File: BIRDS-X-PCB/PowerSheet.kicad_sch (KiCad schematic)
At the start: 31 parts, among them J201 Conn_01x02, J202 Conn_01x02, J203 Conn_01x02, Q201 AO3420, Q202 AO3420, Q502 2N7002, U201 LTC4361-2, U202 LTC4361-2, U203 0.1S7B_0512S3UP

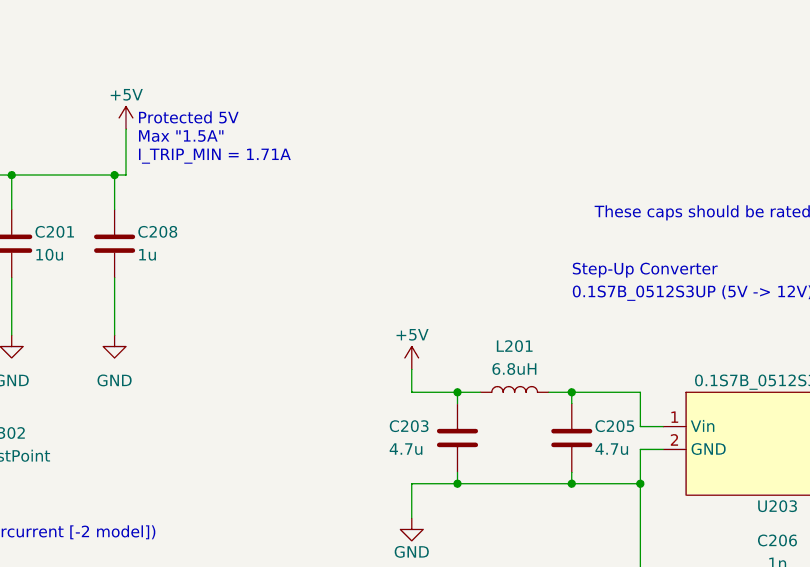
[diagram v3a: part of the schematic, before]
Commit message: Add 12V disable
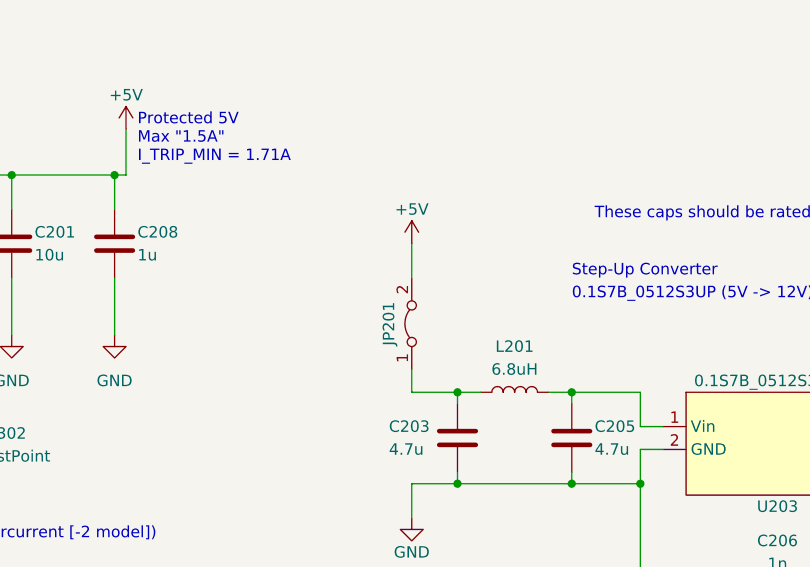
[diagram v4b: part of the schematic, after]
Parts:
- added JP201: Jumper_2_Open, Jumper:SolderJumper-2_P1.3mm_Open_RoundedPad1.0x1.5mm, symbol Jumper:Jumper_2_Bridged
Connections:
- net +5V: now also JP201.2 (B); no longer C203.1, L201.1
- new net: C203.1, JP201.1 (A), L201.1
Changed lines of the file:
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@@
+    (stroke (width 0) (type default))
+  )
+  (wire (pts (xy 161.29 63.5) (xy 161.29 66.04))
     (stroke (width 0) (type default))
   )
@@
     (stroke (width 0) (type default))
   )
-  (wire (pts (xy 161.29 63.5) (xy 161.29 66.04))
+  (wire (pts (xy 161.29 49.53) (xy 161.29 53.34))
     (stroke (width 0) (type default))
   )
@@
         (path "/c2796b15-795a-4d6e-ad4b-0ba87ded4bc9/f0b1214b-f453-423f-b2cf-f5d10e08eafe"
           (reference "#PWR015") (unit 1)
+        )
+      )
+    )
+  )
+  (symbol (lib_id "Jumper:Jumper_2_Bridged") (at 161.29 58.42 90) (unit 1)
+    (in_bom yes) (on_board yes) (dnp no)
+    (property "Reference" "JP201" (at 158.75 58.42 0)
+      (effects (font (size 1.27 1.27)))
+    )
+    (property "Value" "Jumper_2_Open" (at 162.56 60.325 90)
+      (effects (font (size 1.27 1.27)) (justify right) hide)
+    )
+    (property "Footprint" "Jumper:SolderJumper-2_P1.3mm_Open_RoundedPad1.0x1.5mm" (at 161.29 58.42 0)
+      (effects (font (size 1.27 1.27)) hide)
+    )
+    (property "Datasheet" "~" (at 161.29 58.42 0)
+      (effects (font (size 1.27 1.27)) hide)
+    )
+    (pin "1")
+    (pin "2")
+    (instances
+      (project "BIRDS-X-PCB"
+        (path "/c2796b15-795a-4d6e-ad4b-0ba87ded4bc9/f0b1214b-f453-423f-b2cf-f5d10e08eafe"
+          (reference "JP201") (unit 1)
+        )
+        (path "/c2796b15-795a-4d6e-ad4b-0ba87ded4bc9/245c031a-1c72-4f7a-bf07-271990525459"
+          (reference "JP501") (unit 1)
         )
       )
@@
     )
   )
-  (symbol (lib_id "power:+5V") (at 161.29 63.5 0) (unit 1)
-    (in_bom yes) (on_board yes) (dnp no) (fields_autoplaced)
-    (property "Reference" "#PWR07" (at 161.29 67.31 0)
-      (effects (font (size 1.27 1.27)) hide)
-    )
-    (property "Value" "+5V" (at 161.29 59.69 0)
-      (effects (font (size 1.27 1.27)))
-    )
-    (property "Footprint" "" (at 161.29 63.5 0)
-      (effects (font (size 1.27 1.27)) hide)
-    )
-    (property "Datasheet" "" (at 161.29 63.5 0)
-      (effects (font (size 1.27 1.27)) hide)
-    )
+  (symbol (lib_id "power:+5V") (at 161.29 49.53 0) (unit 1)
+    (in_bom yes) (on_board yes) (dnp no) (fields_autoplaced)
+    (property "Reference" "#PWR07" (at 161.29 53.34 0)
+      (effects (font (size 1.27 1.27)) hide)
+    )
+    (property "Value" "+5V" (at 161.29 45.72 0)
+      (effects (font (size 1.27 1.27)))
+    )
+    (property "Footprint" "" (at 161.29 49.53 0)
+      (effects (font (size 1.27 1.27)) hide)
+    )
+    (property "Datasheet" "" (at 161.29 49.53 0)
+      (effects (font (size 1.27 1.27)) hide)
+    )

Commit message: Prep docs for Rev5.1 release
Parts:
- C206, R203, R204, R205: now not fitted
- J201, J202, J203: now not fitted; now left out of the parts list
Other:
- note removed: "TODO switch to one of these if we can order one"
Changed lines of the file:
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@@
   (paper "USLetter")
   (title_block
-    (rev "Rev5.0")
+    (date "2023-09-07")
+    (rev "Rev5.1")
   )
   (junction (at 68.58 50.8) (diameter 0) (color 0 0 0 0)
@@
   (text "For the LTC4361 (per datasheet page 5):\n    R_SENSE = (0.05V) / I_SENSE"
     (at 15.24 20.32 0)
-    (effects (font (size 1.27 1.27)) (justify left bottom))
-  )
-  (text "TODO switch to one of these if we can order one" (at 193.04 104.14 0)
     (effects (font (size 1.27 1.27)) (justify left bottom))
   )
@@
   )
   (symbol (lib_id "Device:R") (at 213.36 130.81 0) (unit 1)
-    (in_bom yes) (on_board yes) (dnp no) (fields_autoplaced)
+    (in_bom yes) (on_board yes) (dnp yes) (fields_autoplaced)
     (property "Reference" "R204" (at 215.9 129.54 0)
       (effects (font (size 1.27 1.27)) (justify left))
@@
   )
   (symbol (lib_id "Device:R") (at 198.12 130.81 0) (unit 1)
-    (in_bom yes) (on_board yes) (dnp no) (fields_autoplaced)
+    (in_bom yes) (on_board yes) (dnp yes) (fields_autoplaced)
     (property "Reference" "R203" (at 200.66 129.54 0)
       (effects (font (size 1.27 1.27)) (justify left))
@@
   )
   (symbol (lib_id "Connector_Generic:Conn_01x02") (at 180.34 144.78 0) (unit 1)
-    (in_bom yes) (on_board yes) (dnp no) (fields_autoplaced)
+    (in_bom no) (on_board yes) (dnp yes) (fields_autoplaced)
     (property "Reference" "J203" (at 182.88 145.415 0)
       (effects (font (size 1.27 1.27)) (justify left))
@@
   )
   (symbol (lib_id "Connector_Generic:Conn_01x02") (at 180.34 106.68 0) (unit 1)
-    (in_bom yes) (on_board yes) (dnp no) (fields_autoplaced)
+    (in_bom no) (on_board yes) (dnp yes) (fields_autoplaced)
     (property "Reference" "J201" (at 182.88 107.315 0)
       (effects (font (size 1.27 1.27)) (justify left))
@@
   )
   (symbol (lib_id "Device:R") (at 228.6 130.81 0) (unit 1)
-    (in_bom yes) (on_board yes) (dnp no) (fields_autoplaced)
+    (in_bom yes) (on_board yes) (dnp yes) (fields_autoplaced)
     (property "Reference" "R205" (at 231.14 130.175 0)
       (effects (font (size 1.27 1.27)) (justify left))
@@
   )
   (symbol (lib_id "Device:C") (at 201.93 88.9 270) (unit 1)
-    (in_bom yes) (on_board yes) (dnp no)
+    (in_bom yes) (on_board yes) (dnp yes)
     (property "Reference" "C206" (at 201.93 82.55 90)
       (effects (font (size 1.27 1.27)))
@@
   )
   (symbol (lib_id "Connector_Generic:Conn_01x02") (at 180.34 125.73 0) (unit 1)
-    (in_bom yes) (on_board yes) (dnp no) (fields_autoplaced)
+    (in_bom no) (on_board yes) (dnp yes) (fields_autoplaced)
     (property "Reference" "J202" (at 182.88 126.365 0)
       (effects (font (size 1.27 1.27)) (justify left))

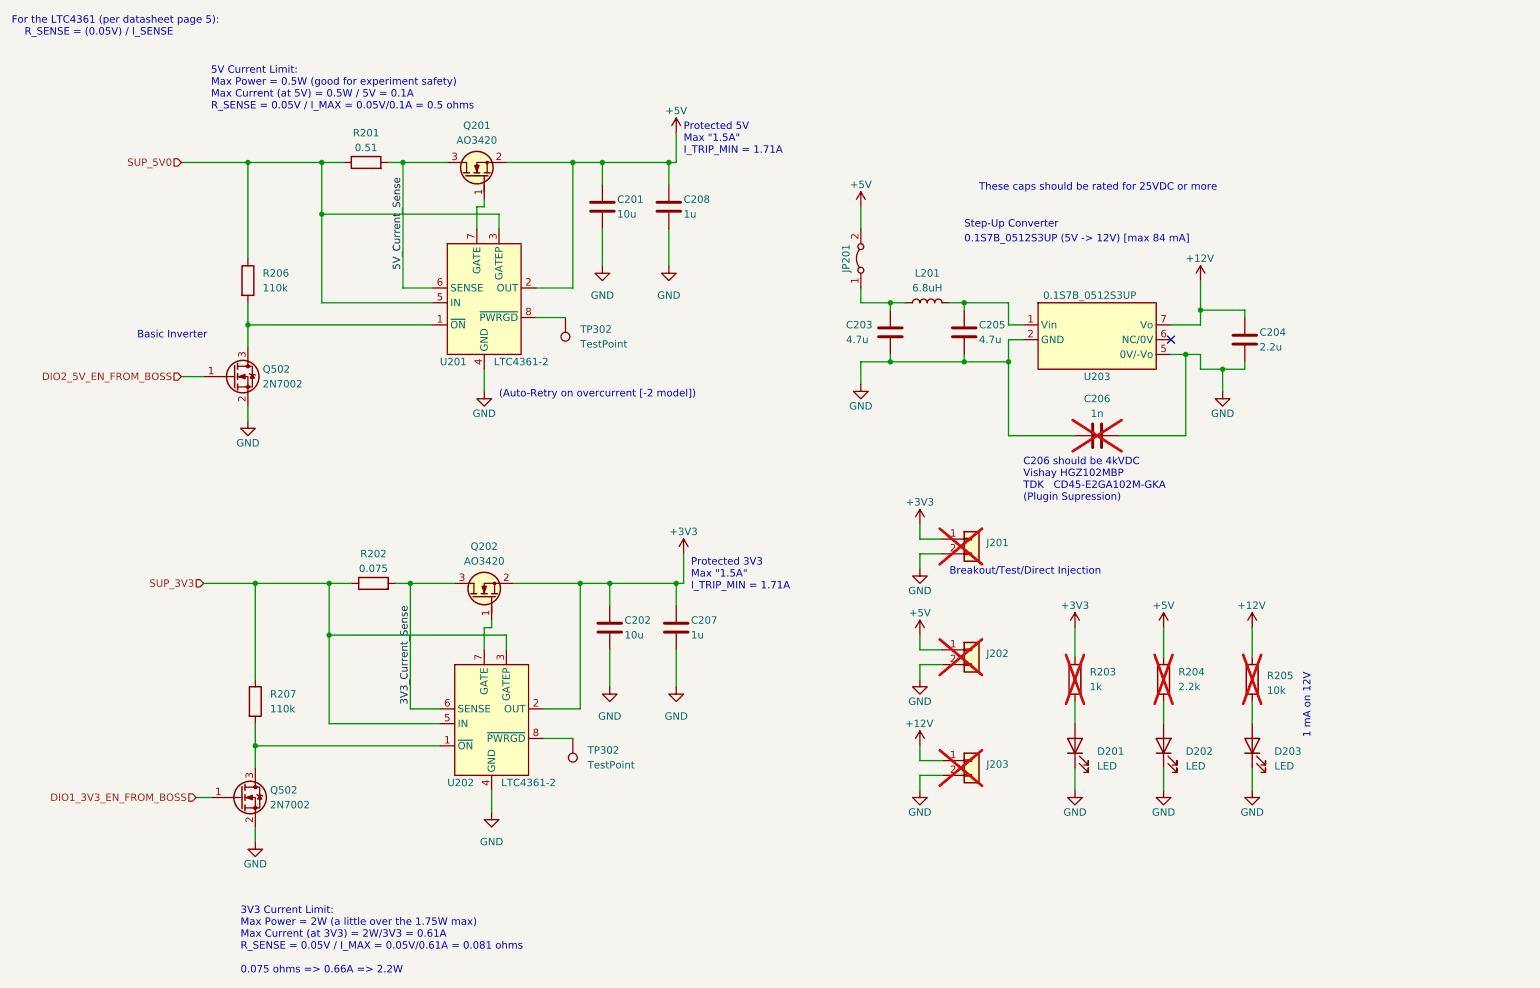
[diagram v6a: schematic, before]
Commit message: Schematic re-work (esp. RADFET fixes)
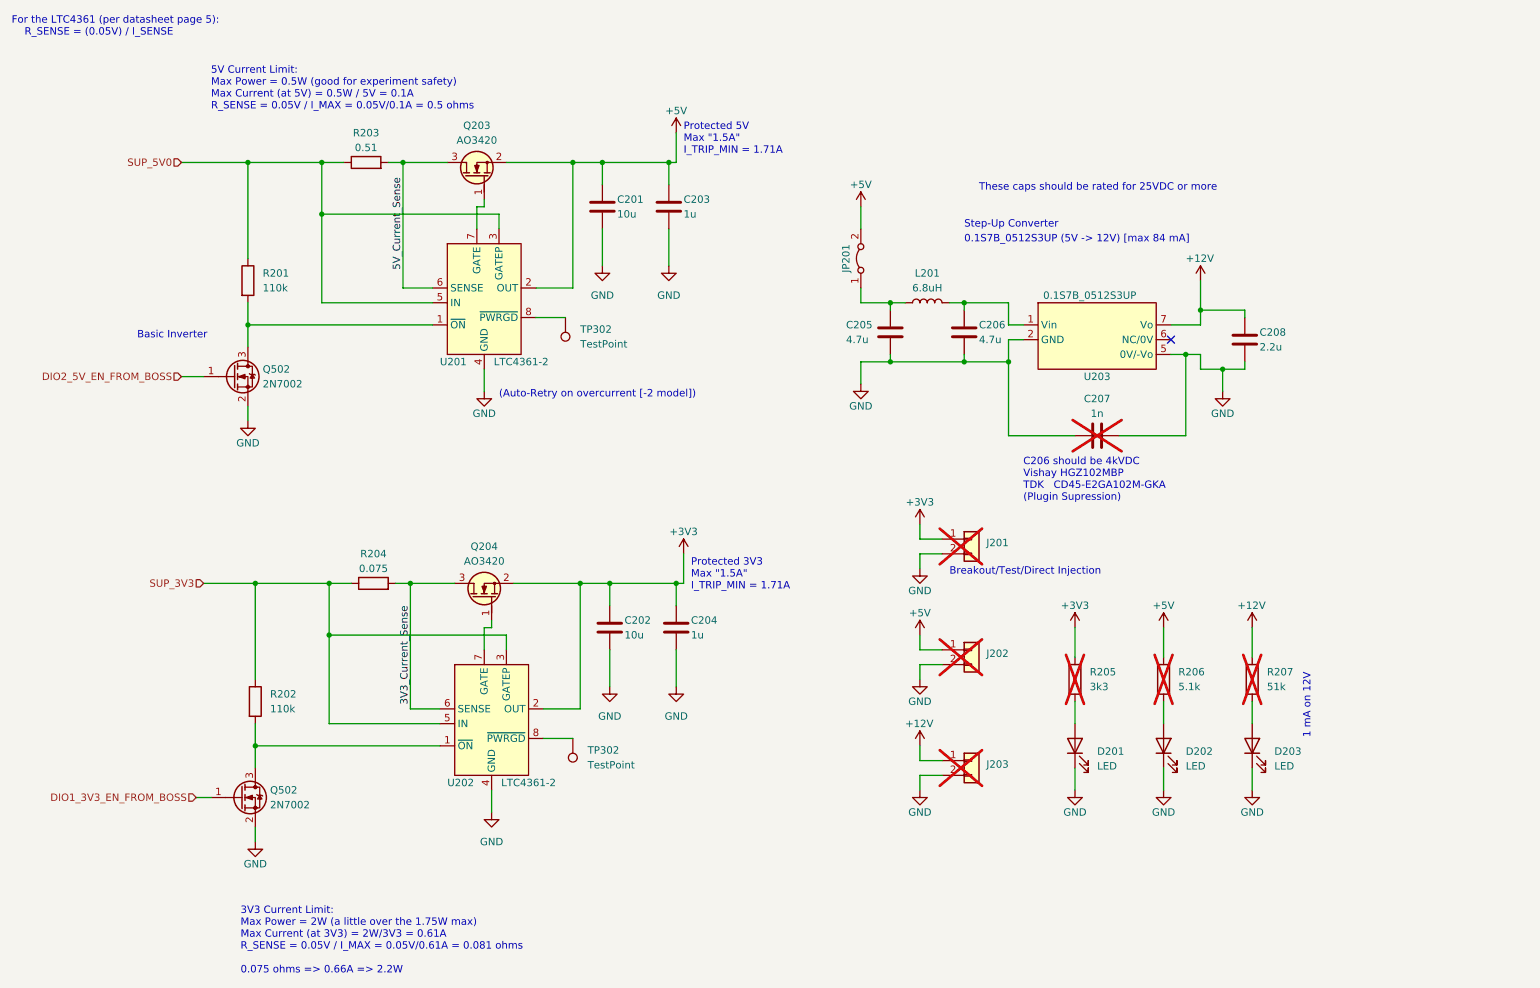
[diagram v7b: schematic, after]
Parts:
- R205: renamed from R203; value 1k -> 3k3
- R206: renamed from R204; value 2.2k -> 5.1k
- R207: renamed from R205; value 10k -> 51k
- renumbered C208 to C203, C207 to C204, C203 to C205, C205 to C206, C206 to C207, C204 to C208, Q201 to Q203, Q202 to Q204, R206 to R201, R207 to R202, R201 to R203, R202 to R204

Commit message: Layout PCB
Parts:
- R205, R206, R207: now fitted
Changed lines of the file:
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@@
   )
   (symbol (lib_id "Device:R") (at 213.36 130.81 0) (unit 1)
-    (in_bom yes) (on_board yes) (dnp yes) (fields_autoplaced)
+    (in_bom yes) (on_board yes) (dnp no) (fields_autoplaced)
     (property "Reference" "R206" (at 215.9 129.54 0)
       (effects (font (size 1.27 1.27)) (justify left))
@@
   )
   (symbol (lib_id "Device:R") (at 198.12 130.81 0) (unit 1)
-    (in_bom yes) (on_board yes) (dnp yes) (fields_autoplaced)
+    (in_bom yes) (on_board yes) (dnp no) (fields_autoplaced)
     (property "Reference" "R205" (at 200.66 129.54 0)
       (effects (font (size 1.27 1.27)) (justify left))
@@
   )
   (symbol (lib_id "Device:R") (at 228.6 130.81 0) (unit 1)
-    (in_bom yes) (on_board yes) (dnp yes) (fields_autoplaced)
+    (in_bom yes) (on_board yes) (dnp no) (fields_autoplaced)
     (property "Reference" "R207" (at 231.14 129.54 0)
       (effects (font (size 1.27 1.27)) (justify left))
